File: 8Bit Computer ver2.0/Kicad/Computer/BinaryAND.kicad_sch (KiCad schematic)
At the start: 4 parts, among them IC5 SN74LVC1G14DBVR, IC6 SN74HCS08DR, IC7 SN74HCS74DR, IC8 SN74ABT821ADWR

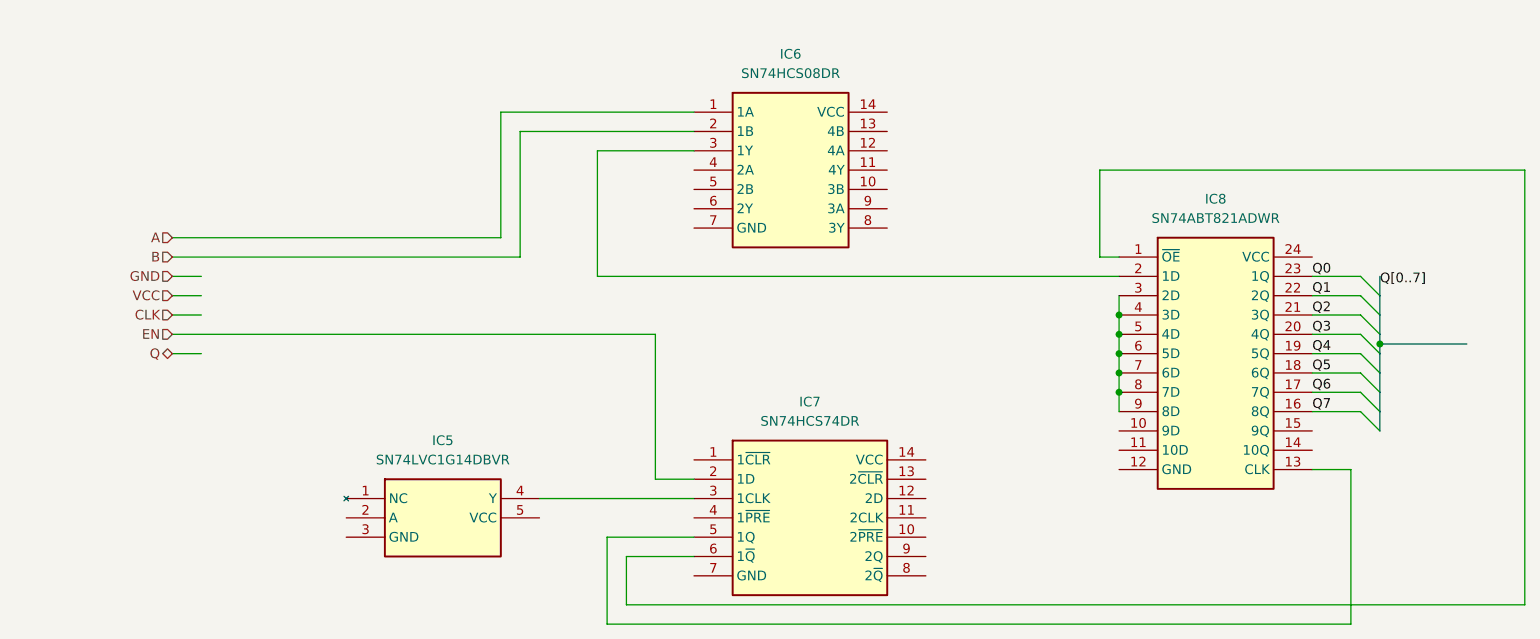
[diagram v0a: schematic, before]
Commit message: parts,Kicad
added 74HCS574 to Kicad
Kicad:
ALU->added Bitwise NOT,OR,XOR,AND
ALU->added A,B 8in OR
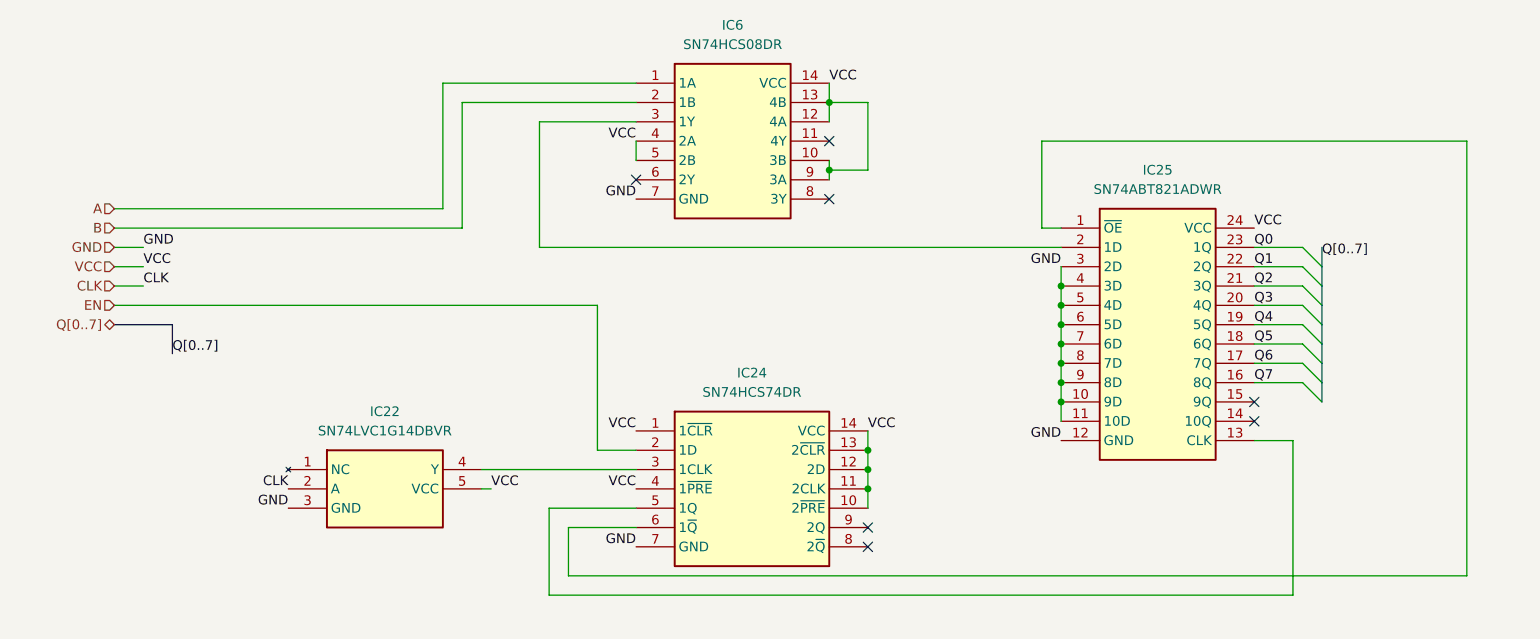
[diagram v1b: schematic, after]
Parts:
- removed IC5: SN74LVC1G14DBVR, Samacsys:SOT95P280X145-5N, symbol Samacsys:SN74LVC1G14DBVR
- removed IC7: SN74HCS74DR, Samacsys:SOIC127P600X175-14N, symbol Samacsys:SN74HCS74DR
- removed IC8: SN74ABT821ADWR, Samacsys:SOIC127P1030X265-24N, symbol Samacsys:SN74ABT821ADWR
- added IC22: SN74LVC1G14DBVR, Samacsys:SOT95P280X145-5N, symbol Samacsys:SN74LVC1G14DBVR
- added IC24: SN74HCS74DR, Samacsys:SOIC127P600X175-14N, symbol Samacsys:SN74HCS74DR
- added IC25: SN74ABT821ADWR, Samacsys:SOIC127P1030X265-24N, symbol Samacsys:SN74ABT821ADWR
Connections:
- net CLK: now also IC22.2 (A)
- net EN: now also IC24.2 (1D)
- net GND: now also IC6.7 (GND), IC22.3 (GND), IC24.7 (GND), IC25.10 (9D), IC25.11 (10D), IC25.12 (GND), IC25.3 (2D), IC25.4 (3D), IC25.5 (4D), IC25.6 (5D), IC25.7 (6D), IC25.8 (7D), IC25.9 (8D)
- net Q0: now also IC25.23 (1Q)
- net Q1: now also IC25.22 (2Q)
- net Q2: now also IC25.21 (3Q)
- net Q3: now also IC25.20 (4Q)
- net Q4: now also IC25.19 (5Q)
- net Q5: now also IC25.18 (6Q)
- net Q6: now also IC25.17 (7Q)
- net Q7: now also IC25.16 (8Q)
- net VCC: now also IC6.10 (3B), IC6.12 (4A), IC6.13 (4B), IC6.14 (VCC), IC6.4 (2A), IC6.5 (2B), IC6.9 (3A), IC22.5 (VCC), IC24.1 (1~{CLR}), IC24.10 (2~{PRE}), IC24.11 (2CLK), IC24.12 (2D), IC24.13 (2~{CLR}), IC24.14 (VCC), IC24.4 (1~{PRE}), IC25.24 (VCC)
- net at IC6.3 (1Y): now also IC25.2 (1D)
- new net: IC24.6 (1~{Q}), IC25.1 (~{OE})
- new net: IC24.5 (1Q), IC25.13 (CLK)
- new net: IC22.4 (Y), IC24.3 (1CLK)
- no-connect marks 0 -> 7
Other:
- moved on the sheet: IC6

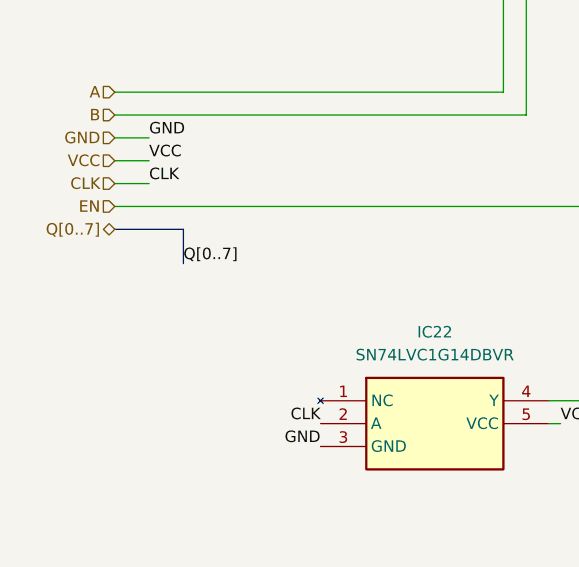
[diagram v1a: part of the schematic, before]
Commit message: Kicad,parts
Kicad:
added FlagRegister
began Inc, Comp
parts:
added comparator for P>Q 682
added faster sram 12ns AS7C
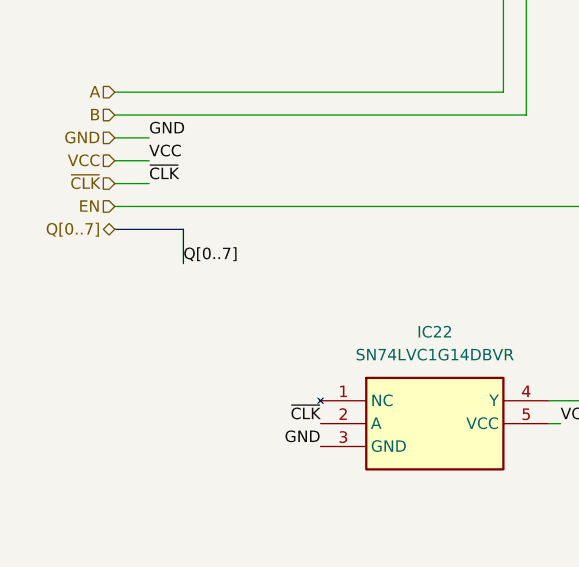
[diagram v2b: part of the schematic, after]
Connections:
- net CLK renamed ~{CLK}
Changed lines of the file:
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@@
 		)
 	)
-	(label "CLK"
+	(label "~{CLK}"
 		(at 62.23 109.22 180)
 		(effects
@@
 		)
 	)
-	(label "CLK"
+	(label "~{CLK}"
 		(at 43.18 82.55 0)
 		(effects
@@
 		)
 	)
-	(hierarchical_label "CLK"
+	(hierarchical_label "~{CLK}"
 		(shape input)
 		(at 39.37 82.55 180)

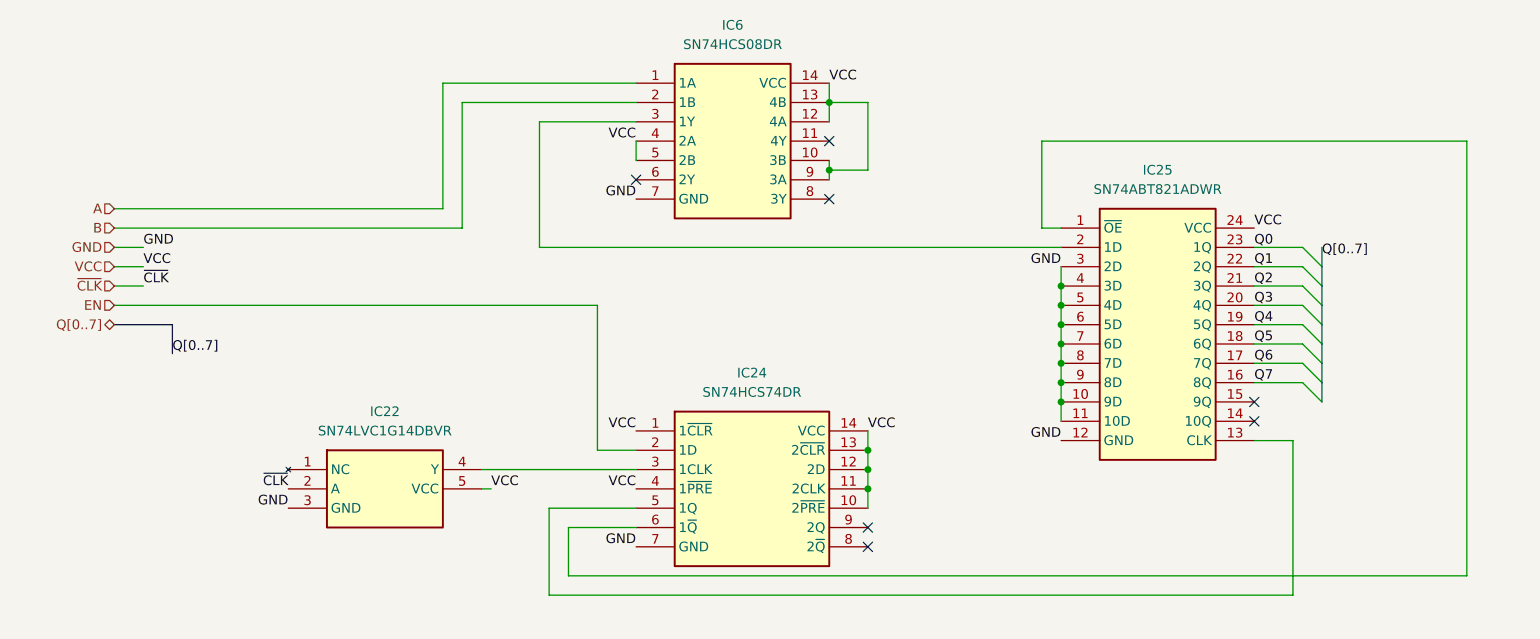
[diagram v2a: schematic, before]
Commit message: parts,Kicad
parts:
changed 8xDlatch HCS to ABT 574
waiting for SRAM CAD Model
Kicad:
imported AHC types of ICs
added ProgrammeCounter
finished Comparator
changed all HCS to AHC except 3in OR ->no AHC Version
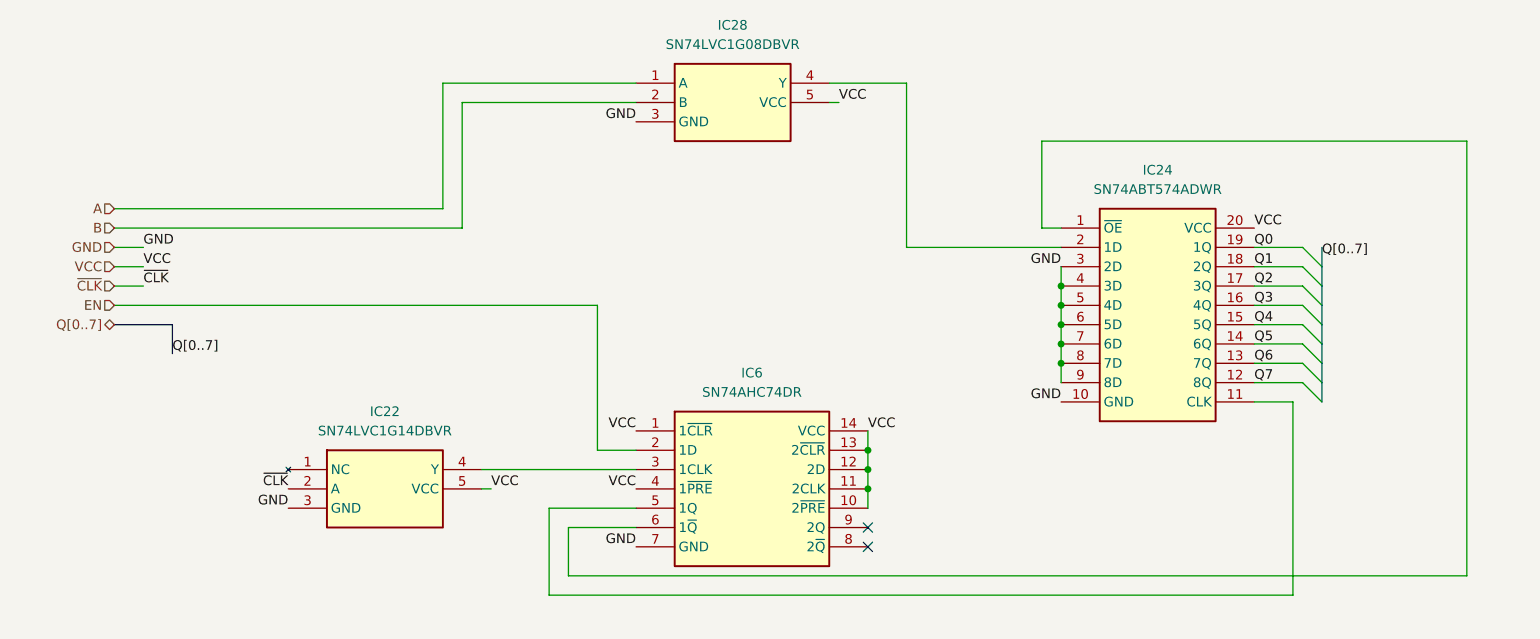
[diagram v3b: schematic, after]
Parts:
- removed IC24: SN74HCS74DR, Samacsys:SOIC127P600X175-14N, symbol Samacsys:SN74HCS74DR
- removed IC25: SN74ABT821ADWR, Samacsys:SOIC127P1030X265-24N, symbol Samacsys:SN74ABT821ADWR
- removed IC6: SN74HCS08DR, Samacsys:SOIC127P600X175-14N, symbol Samacsys:SN74HCS08DR
- added IC24: SN74ABT574ADWR, Samacsys:SOIC127P1030X265-20N, symbol Samacsys:SN74ABT574ADWR
- added IC28: SN74LVC1G08DBVR, Samacsys:SOT95P280X145-5N, symbol Samacsys:SN74LVC1G08DBVR
- added IC6: SN74AHC74DR, Samacsys:SOIC127P600X175-14N, symbol Samacsys:SN74AHC74DR
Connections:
- net A: now also IC28.1 (A)
- net B: now also IC28.2 (B)
- net EN: now also IC6.2 (1D)
- net GND: now also IC24.10 (GND), IC24.3 (2D), IC24.4 (3D), IC24.5 (4D), IC24.6 (5D), IC24.7 (6D), IC24.8 (7D), IC24.9 (8D), IC28.3 (GND), IC6.7 (GND)
- net Q0: now also IC24.19 (1Q)
- net Q1: now also IC24.18 (2Q)
- net Q2: now also IC24.17 (3Q)
- net Q3: now also IC24.16 (4Q)
- net Q4: now also IC24.15 (5Q)
- net Q5: now also IC24.14 (6Q)
- net Q6: now also IC24.13 (7Q)
- net Q7: now also IC24.12 (8Q)
- net VCC: now also IC24.20 (VCC), IC28.5 (VCC), IC6.1 (1~{CLR}), IC6.10 (2~{PRE}), IC6.11 (2CLK), IC6.12 (2D), IC6.13 (2~{CLR}), IC6.14 (VCC), IC6.4 (1~{PRE})
- net at IC22.4 (Y): now also IC6.3 (1CLK)
- new net: IC24.11 (CLK), IC6.5 (1Q)
- new net: IC24.1 (~{OE}), IC6.6 (1~{Q})
- new net: IC24.2 (1D), IC28.4 (Y)
- no-connect marks 7 -> 2

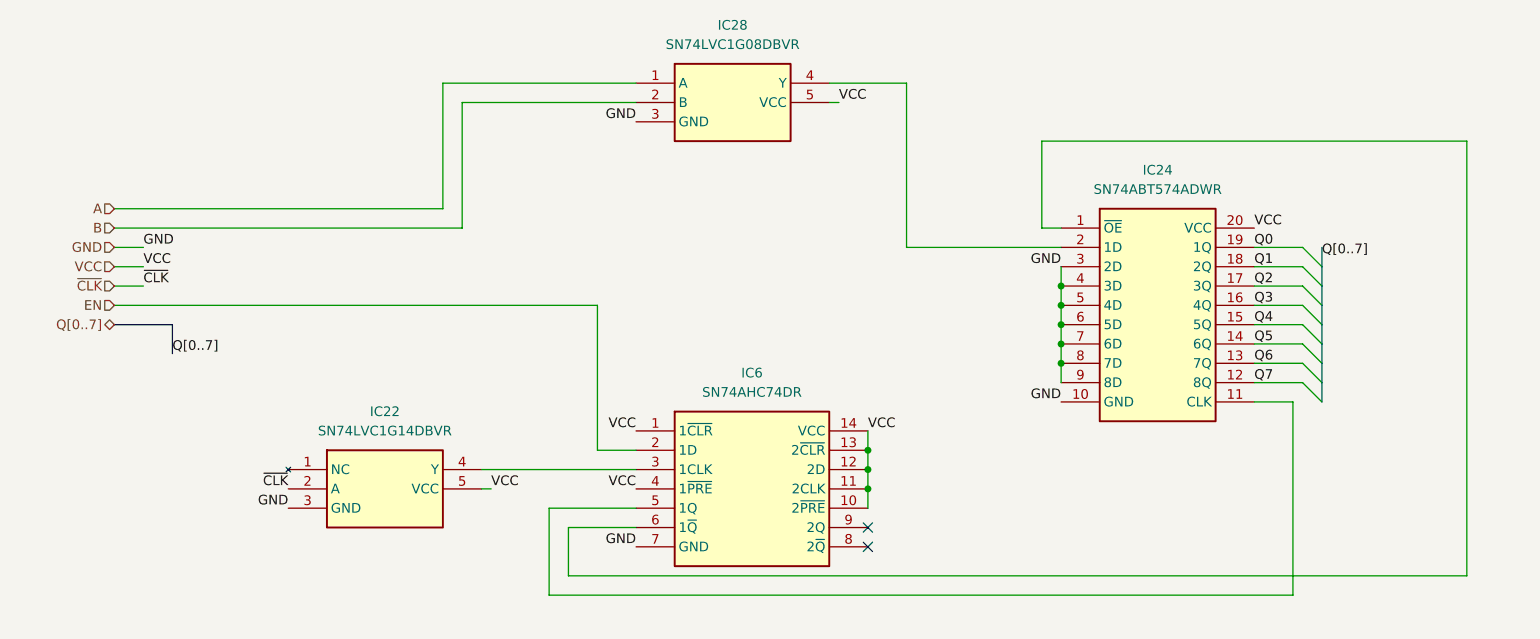
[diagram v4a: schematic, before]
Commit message: Kicad, parts
Parts:
added Leds
Kicad:
added Input Output
changed Q bus to DAT bus
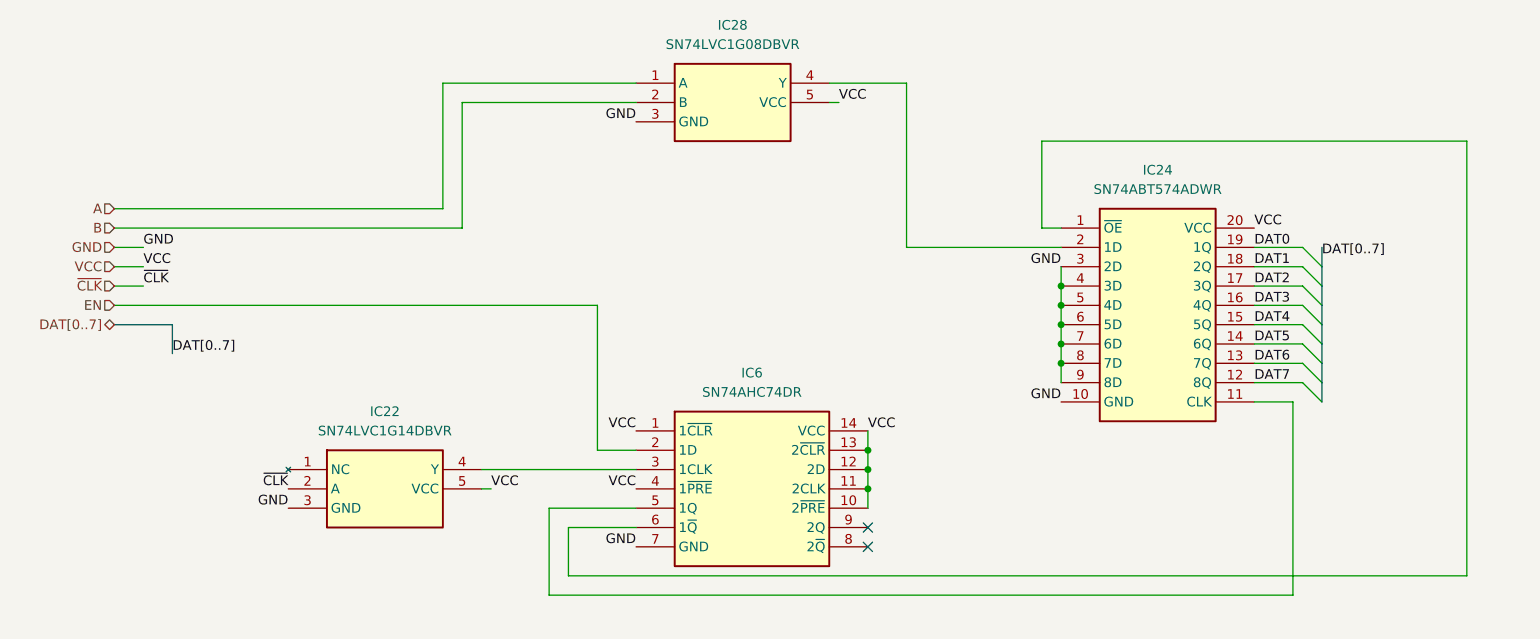
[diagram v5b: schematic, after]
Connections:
- net Q0 renamed DAT0
- net Q1 renamed DAT1
- net Q2 renamed DAT2
- net Q3 renamed DAT3
- net Q4 renamed DAT4
- net Q5 renamed DAT5
- net Q6 renamed DAT6
- net Q7 renamed DAT7
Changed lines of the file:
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@@
 		)
 	)
-	(label "Q6"
+	(label "DAT6"
 		(at 189.23 92.71 0)
 		(effects
@@
 		)
 	)
-	(label "Q2"
+	(label "DAT2"
 		(at 189.23 82.55 0)
 		(effects
@@
 		)
 	)
-	(label "Q3"
+	(label "DAT3"
 		(at 189.23 85.09 0)
 		(effects
@@
 		)
 	)
-	(label "Q1"
+	(label "DAT1"
 		(at 189.23 80.01 0)
 		(effects
@@
 		)
 	)
-	(label "Q7"
+	(label "DAT7"
 		(at 189.23 95.25 0)
 		(effects
@@
 		)
 	)
-	(label "Q0"
+	(label "DAT0"
 		(at 189.23 77.47 0)
 		(effects
@@
 		)
 	)
-	(label "Q[0..7]"
+	(label "DAT[0..7]"
 		(at 198.12 78.74 0)
 		(effects
@@
 		)
 	)
-	(label "Q5"
+	(label "DAT5"
 		(at 189.23 90.17 0)
 		(effects
@@
 		)
 	)
-	(label "Q[0..7]"
+	(label "DAT[0..7]"
 		(at 46.99 91.44 0)
 		(effects
@@
 		)
 	)
-	(label "Q4"
+	(label "DAT4"
 		(at 189.23 87.63 0)
 		(effects
@@
 		)
 	)
-	(hierarchical_label "Q[0..7]"
+	(hierarchical_label "DAT[0..7]"
 		(shape tri_state)
 		(at 39.37 87.63 180)

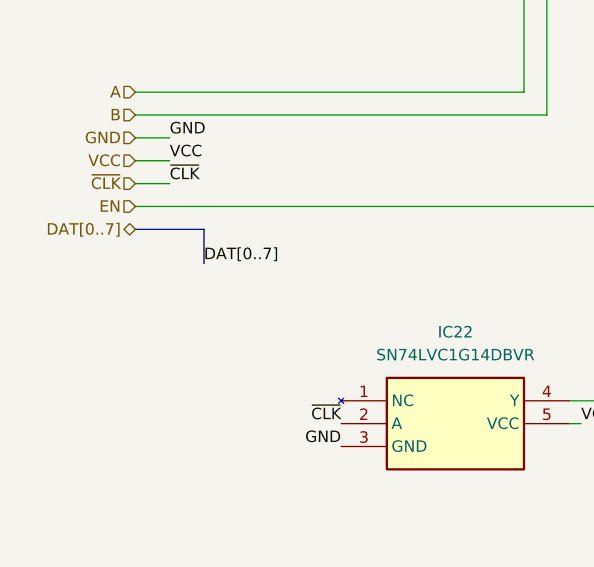
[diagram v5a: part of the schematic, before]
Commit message: Kicad, parts
parts:
added USB C PD Triggerboard
added Delay Chip for 90ns
added Push Button
Kicad:
added USB C PD Triggerboard
added rising edge detector via Delay and Xor for Accept Push Button
added VBUS net
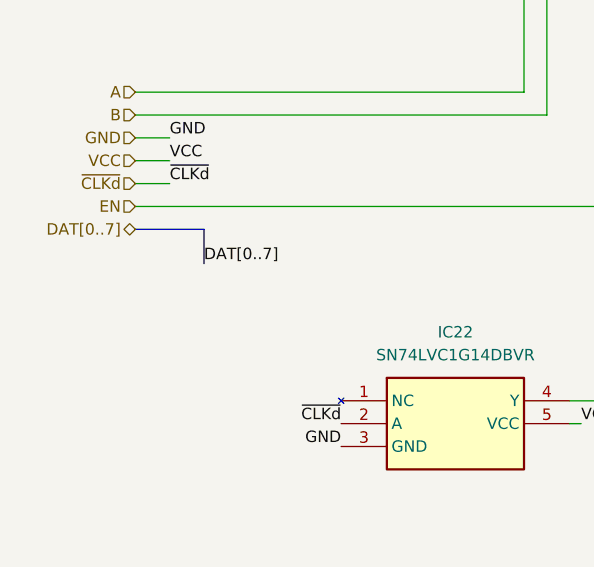
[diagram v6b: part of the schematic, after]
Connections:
- net ~{CLK} renamed ~{CLKd}
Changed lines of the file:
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@@
 		)
 	)
-	(label "~{CLK}"
+	(label "~{CLKd}"
 		(at 62.23 109.22 180)
 		(effects
@@
 		)
 	)
-	(label "~{CLK}"
+	(label "~{CLKd}"
 		(at 43.18 82.55 0)
 		(effects
@@
 		)
 	)
-	(hierarchical_label "~{CLK}"
+	(hierarchical_label "~{CLKd}"
 		(shape input)
 		(at 39.37 82.55 180)
